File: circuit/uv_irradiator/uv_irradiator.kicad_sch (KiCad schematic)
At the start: 47 parts, among them J1 Jack-DC, M1 PUDC12Z4, Q1 2SK4017, Q2 2SC2712, Q3 IRFU9024NPBF, SW1 TBD, SW2 TBD, SW3 TBD, SW4 ON, U1 TA48M05F_HSIP3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

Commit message: port changed
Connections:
- net GND: now also U2.5 (+); no longer U2.6 (-)
- net ~{SW1}: now reaches R5.1, SW2.2
- net ~{SW1}: now also A1.25 (GPIO19); no longer A1.22 (GPIO17)
- net ~{SW0}: now reaches R4.1, SW1.2
- net ~{SW0}: now also A1.24 (GPIO18); no longer A1.21 (GPIO16)
- net VPOT: now reaches A1.29 (GPIO22), RV1.1
- net APOT: now reaches A1.31 (GPIO26_ADC0), RV1.2
- net ~{SW2}: now reaches R6.1, SW3.2
- net ~{SW2}: now also A1.26 (GPIO20); no longer A1.24 (GPIO18)
- net at A1.19 (GPIO14): no longer U4.1 (SDA)
- net at A1.20 (GPIO15): no longer U4.2 (SCL)
- net at U2.7: now also U2.6 (-); no longer U2.5 (+)
- net OUT_ENA renamed SW3
- net VCRNT renamed ACRNT
- net VTEMP renamed ATEMP
- new net: Q3.1 (D), U10. (LED-), U5. (LED-), U6. (LED-), U7. (LED-), U8. (LED-), U9. (LED-)
- new net SCL: A1.22 (GPIO17), U4.2 (SCL)
- new net SDA: A1.21 (GPIO16), U4.1 (SDA)
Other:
- moved on the sheet: RV1

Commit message: update schematic
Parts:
- added C6: 0.1u, symbol Device:C_Small
- added D10: Red, symbol Device:LED_Small
- added D11: Blue, symbol Device:LED_Small
- added R12: 10k, symbol Device:R_Small
- added R13, R14: 470, symbol Device:R_Small
- C4: value 1u -> 4.7u
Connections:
- net ACRNT: now also A1.32 (GPIO27_ADC1); no longer A1.34 (GPIO28_ADC2)
- net ATEMP: now also A1.34 (GPIO28_ADC2), C6.2, R12.2; no longer A1.32 (GPIO27_ADC1)
- net FAN_PWM: now also A1.14 (GPIO10); no longer A1.5 (GPIO3)
- net GND: now also C6.1, D10.1 (K), D11.1 (K), R12.1
- net ~{SW0}: now also A1.26 (GPIO20); no longer A1.24 (GPIO18)
- net ~{SW2}: now also A1.24 (GPIO18); no longer A1.26 (GPIO20)
- net LED_OUT: now reaches A1.4 (GPIO2)
- net LED_OUT: now also R14.2
- new net: D10.2 (A), R13.1
- new net: Q3.1 (D), U10. (LED-), U5. (LED-), U6. (LED-), U7. (LED-), U8. (LED-), U9. (LED-)
- new net: D11.2 (A), R14.1
- new net LED_ERR: A1.5 (GPIO3), R13.2
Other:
- moved on the sheet: A1, C5, D1, R4, R5, R6, R7, RV1, SW1, SW2, SW3, SW4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

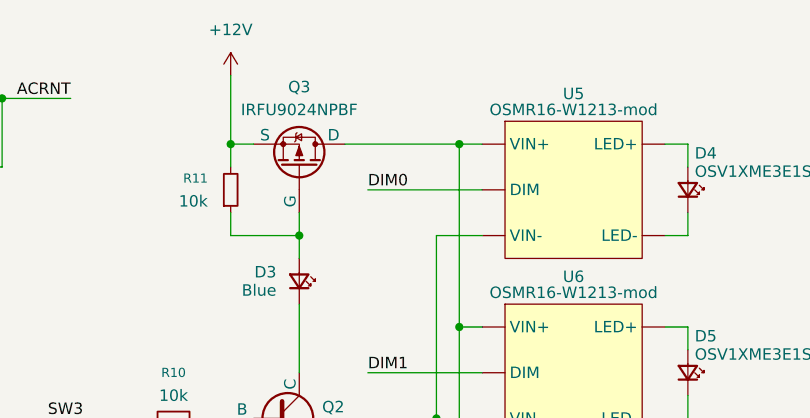
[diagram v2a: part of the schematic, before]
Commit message: update schematic
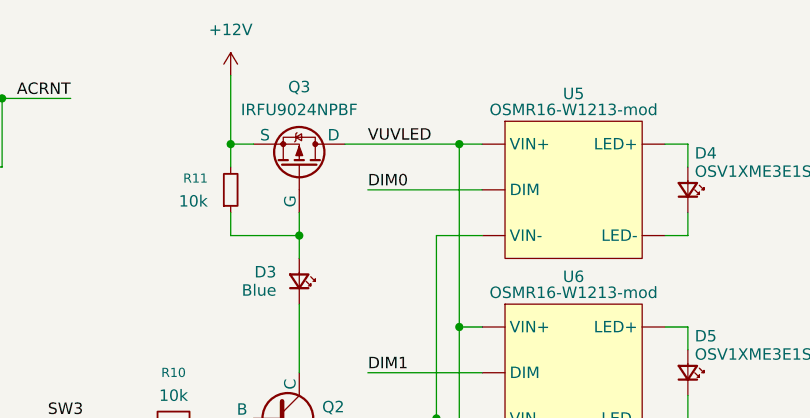
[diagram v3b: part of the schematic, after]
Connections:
- net VUVLED: now reaches Q3.1 (D), U10. (LED-), U5. (LED-), U6. (LED-), U7. (LED-), U8. (LED-), U9. (LED-)
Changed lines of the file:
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@@
+		)
+	)
+	(label "VUVLED"
+		(at 200.66 30.48 0)
+		(effects
+			(font
+				(size 1.27 1.27)
+			)
+			(justify left bottom)
 		)
 	)
